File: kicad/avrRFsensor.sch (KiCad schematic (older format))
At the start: 26 parts, among them P1 CONN_1, P2 CONN_1, P3 CONN_1, P4 CONN_1, P5 CONN_1, P6 CONN_1, U1 ATMEGA168PA-A, U2 RFM69, X1 18MHz HC49USSMD

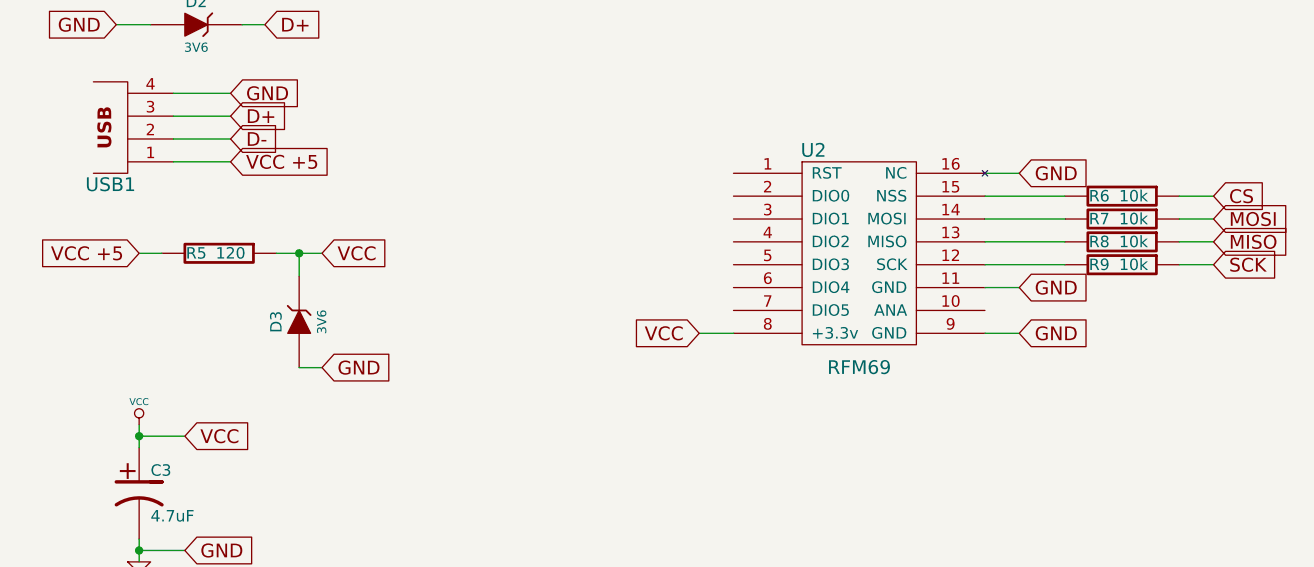
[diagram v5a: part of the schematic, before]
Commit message: fixed schematics. Working hidtool, transmit and read RFM registers in test mode.
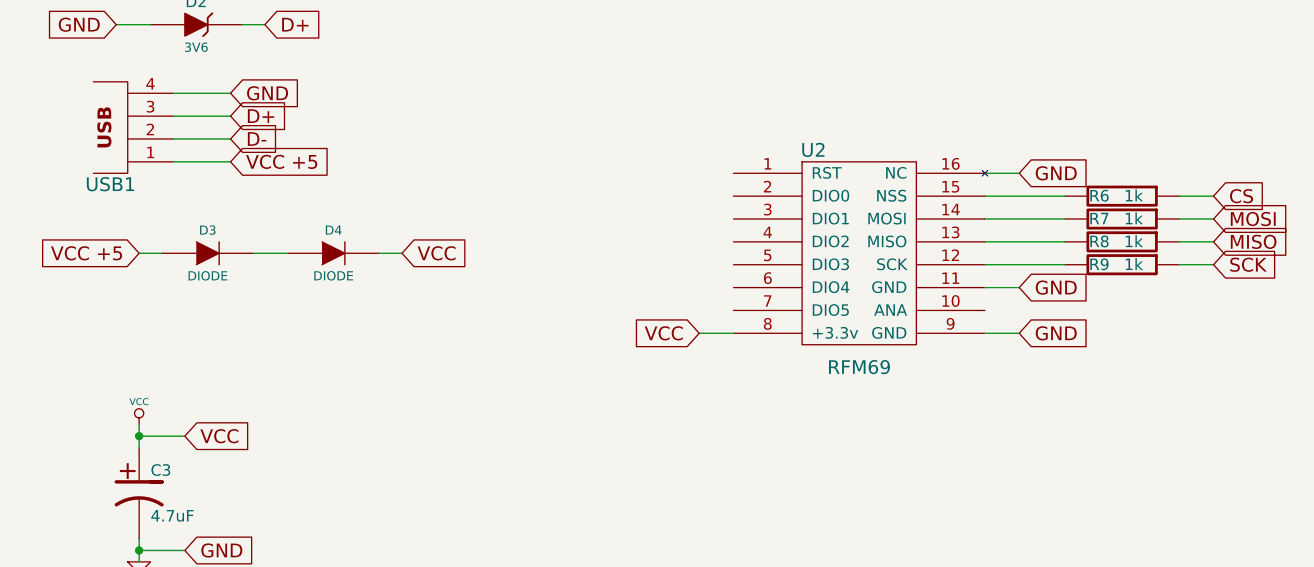
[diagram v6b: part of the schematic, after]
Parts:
- removed D3: 3V6, symbol ZENER
- removed R5: 120, symbol R
- added D3, D4: DIODE, ~, symbol DIODE
- R6, R7, R8, R9: value 10k -> 1k
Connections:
- net VCC: now also D4.2 (K)
- net VCC +5: now also D3.1 (A)
- new net: D3.2 (K), D4.1 (A)
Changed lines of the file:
@@
 Sheet 1 1
 Title ""
-Date "26 jan 2015"
+Date "7 feb 2015"
 Rev ""
 Comp ""
@@
 $EndComp
 $Comp
-L GND #PWR01
+L GND #PWR2
 U 1 1 4E041C8A
 P 1050 7350
-F 0 "#PWR01" H 1050 7350 30  0001 C CNN
+F 0 "#PWR2" H 1050 7350 30  0001 C CNN
 F 1 "GND" H 1050 7280 30  0001 C CNN
 F 2 "" H 1050 7350 60  0001 C CNN
@@
 Connection ~ 1050 6800
 $Comp
-L VCC #PWR02
+L VCC #PWR1
 U 1 1 54B791F6
 P 1050 6750
-F 0 "#PWR02" H 1050 6850 30  0001 C CNN
+F 0 "#PWR1" H 1050 6850 30  0001 C CNN
 F 1 "VCC" H 1050 6850 30  0000 C CNN
 F 2 "" H 1050 6750 60  0000 C CNN
@@
 P 5350 5850
 F 0 "R7" V 5350 5750 50  0000 C CNN
-F 1 "10k" V 5350 5900 50  0000 C CNN
+F 1 "1k" V 5350 5900 50  0000 C CNN
 F 2 "" H 5350 5850 60  0001 C CNN
 F 3 "" H 5350 5850 60  0001 C CNN
@@
 P 5350 5950
 F 0 "R8" V 5350 5850 50  0000 C CNN
-F 1 "10k" V 5350 6000 50  0000 C CNN
+F 1 "1k" V 5350 6000 50  0000 C CNN
 F 2 "" H 5350 5950 60  0001 C CNN
 F 3 "" H 5350 5950 60  0001 C CNN
@@
 P 5350 6050
 F 0 "R9" V 5350 5950 50  0000 C CNN
-F 1 "10k" V 5350 6100 50  0000 C CNN
+F 1 "1k" V 5350 6100 50  0000 C CNN
 F 2 "" H 5350 6050 60  0001 C CNN
 F 3 "" H 5350 6050 60  0001 C CNN
@@
 Text GLabel 1050 6000 0    60   Input ~ 0
 VCC +5
-$Comp
-L R R5
-U 1 1 54B7D03F
-P 1400 6000
-F 0 "R5" V 1400 5900 50  0000 C CNN
-F 1 "120" V 1400 6050 50  0000 C CNN
-F 2 "" H 1400 6000 60  0001 C CNN
-F 3 "" H 1400 6000 60  0001 C CNN
-	1    1400 6000
-	0    1    1    0
-$EndComp
-$Comp
-L ZENER D3
-U 1 1 54B7D045
-P 1750 6300
-F 0 "D3" H 1750 6400 50  0000 C CNN
-F 1 "3V6" H 1750 6200 40  0000 C CNN
-F 2 "" H 1750 6300 60  0001 C CNN
-F 3 "" H 1750 6300 60  0001 C CNN
-	1    1750 6300
-	0    -1   -1   0
-$EndComp
-Text GLabel 1850 6000 2    60   Input ~ 0
+Text GLabel 2200 6000 2    60   Input ~ 0
 VCC
 Wire Wire Line
 	1050 6000 1150 6000
-Wire Wire Line
-	1650 6000 1850 6000
-Wire Wire Line
-	1750 6100 1750 6000
-Connection ~ 1750 6000
-Text GLabel 1850 6500 2    60   Input ~ 0
-GND
-Wire Wire Line
-	1750 6500 1850 6500
 $Comp
 L R R6
@@
 P 5350 5750
 F 0 "R6" V 5350 5650 50  0000 C CNN
-F 1 "10k" V 5350 5800 50  0000 C CNN
+F 1 "1k" V 5350 5800 50  0000 C CNN
 F 2 "" H 5350 5750 60  0001 C CNN
 F 3 "" H 5350 5750 60  0001 C CNN
@@
 Wire Wire Line
 	6300 4600 5300 4600
+$Comp
+L DIODE D3
+U 1 1 54D5C585
+P 1350 6000
+F 0 "D3" H 1350 6100 40  0000 C CNN
+F 1 "DIODE" H 1350 5900 40  0000 C CNN
+F 2 "~" H 1350 6000 60  0000 C CNN
+F 3 "~" H 1350 6000 60  0000 C CNN
+	1    1350 6000
+	1    0    0    -1
+$EndComp
+$Comp
+L DIODE D4
+U 1 1 54D5C594
+P 1900 6000
+F 0 "D4" H 1900 6100 40  0000 C CNN
+F 1 "DIODE" H 1900 5900 40  0000 C CNN
+F 2 "~" H 1900 6000 60  0000 C CNN
+F 3 "~" H 1900 6000 60  0000 C CNN
+	1    1900 6000
+	1    0    0    -1
+$EndComp
+Wire Wire Line
+	1550 6000 1700 6000
+Wire Wire Line
+	2100 6000 2200 6000
 $EndSCHEMATC

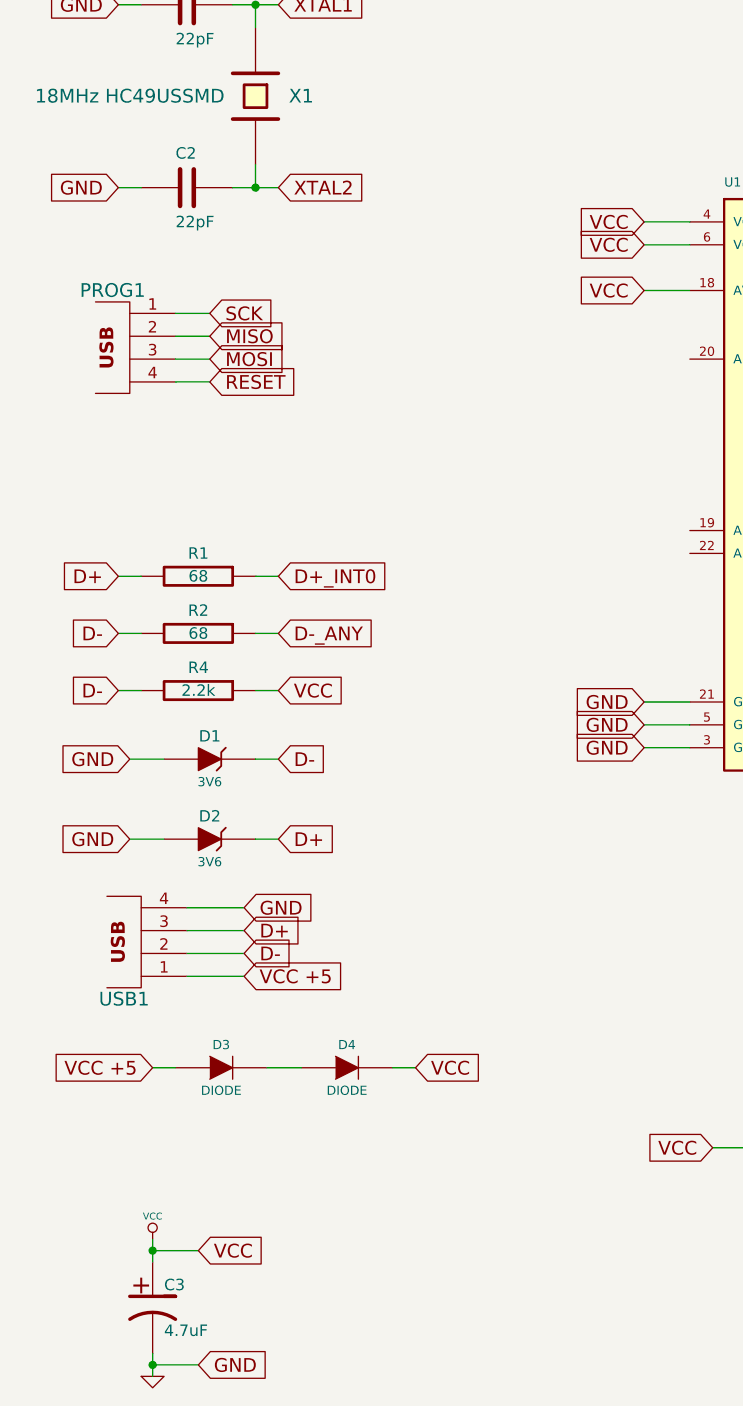
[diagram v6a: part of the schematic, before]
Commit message: No diodes inside module. They are now in the cable. So device should not be used directly in the USB port of computer.
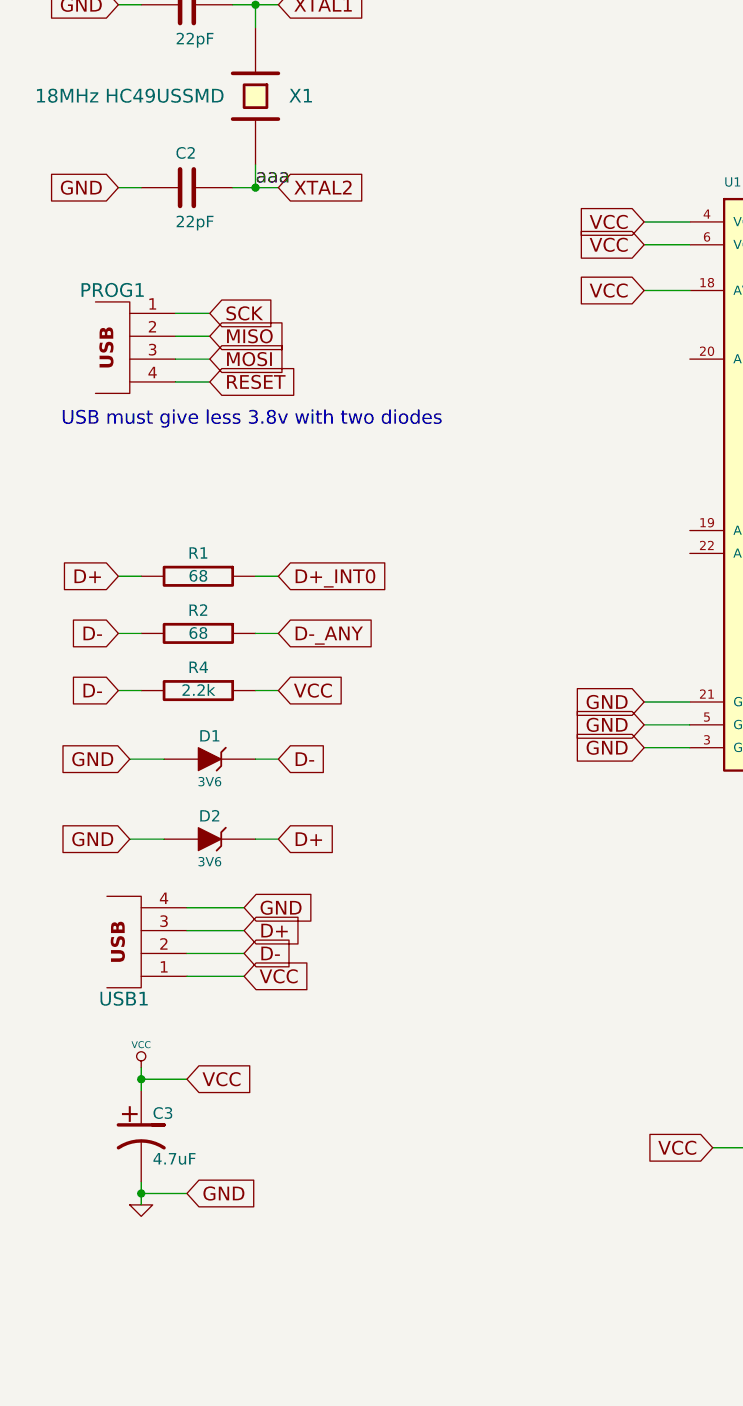
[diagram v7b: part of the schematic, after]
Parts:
- removed D3, D4: DIODE, ~, symbol DIODE
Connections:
- net VCC +5 is gone; now on net VCC: USB1.1
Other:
- note added: "USB must give less 3.8v with two diodes"
- moved on the sheet: C3
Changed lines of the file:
@@
 Sheet 1 1
 Title ""
-Date "7 feb 2015"
+Date "10 feb 2015"
 Rev ""
 Comp ""
@@
 Wire Wire Line
 	1500 1350 1500 1450
-Connection ~ 1050 7300
+Connection ~ 1000 6550
 Wire Wire Line
 	950  4650 1100 4650
@@
 L GND #PWR2
 U 1 1 4E041C8A
-P 1050 7350
-F 0 "#PWR2" H 1050 7350 30  0001 C CNN
-F 1 "GND" H 1050 7280 30  0001 C CNN
-F 2 "" H 1050 7350 60  0001 C CNN
-F 3 "" H 1050 7350 60  0001 C CNN
-	1    1050 7350
+P 1000 6600
+F 0 "#PWR2" H 1000 6600 30  0001 C CNN
+F 1 "GND" H 1000 6530 30  0001 C CNN
+F 2 "" H 1000 6600 60  0001 C CNN
+F 3 "" H 1000 6600 60  0001 C CNN
+	1    1000 6600
 	1    0    0    -1
 $EndComp
@@
 L CP1 C3
 U 1 1 4B61D8DC
-P 1050 7050
-F 0 "C3" H 1100 7150 50  0000 L CNN
-F 1 "4.7uF" H 1100 6950 50  0000 L CNN
-F 2 "" H 1050 7050 60  0001 C CNN
-F 3 "" H 1050 7050 60  0001 C CNN
-	1    1050 7050
+P 1000 6300
+F 0 "C3" H 1050 6400 50  0000 L CNN
+F 1 "4.7uF" H 1050 6200 50  0000 L CNN
+F 2 "" H 1000 6300 60  0001 C CNN
+F 3 "" H 1000 6300 60  0001 C CNN
+	1    1000 6300
 	1    0    0    -1
 $EndComp
@@
 	1    0    0    -1
 $EndComp
-Text GLabel 1250 6800 2    60   Input ~ 0
+Text GLabel 1200 6050 2    60   Input ~ 0
 VCC
 Text GLabel 1600 4350 2    60   Input ~ 0
@@
 Wire Wire Line
 	1000 1000 1100 1000
-Text GLabel 1250 7300 2    60   Input ~ 0
+Text GLabel 1200 6550 2    60   Input ~ 0
 GND
 Text GLabel 900  1350 0    60   Input ~ 0
@@
 MOSI
 Wire Wire Line
-	1050 7250 1050 7350
-Wire Wire Line
-	1050 6750 1050 6850
-Connection ~ 1050 6800
+	1000 6500 1000 6600
+Wire Wire Line
+	1000 6000 1000 6100
+Connection ~ 1000 6050
 $Comp
 L VCC #PWR1
 U 1 1 54B791F6
-P 1050 6750
-F 0 "#PWR1" H 1050 6850 30  0001 C CNN
-F 1 "VCC" H 1050 6850 30  0000 C CNN
-F 2 "" H 1050 6750 60  0000 C CNN
-F 3 "" H 1050 6750 60  0000 C CNN
-	1    1050 6750
+P 1000 6000
+F 0 "#PWR1" H 1000 6100 30  0001 C CNN
+F 1 "VCC" H 1000 6100 30  0000 C CNN
+F 2 "" H 1000 6000 60  0000 C CNN
+F 3 "" H 1000 6000 60  0000 C CNN
+	1    1000 6000
 	1    0    0    -1
 $EndComp
@@
 	1500 3850 1600 3850
 Text GLabel 1450 5600 2    60   Input ~ 0
-VCC +5
+VCC
 Text GLabel 1450 5300 2    60   Input ~ 0
 GND
@@
 	5500 2900 5300 2900
 Wire Wire Line
-	1250 7300 1050 7300
-Wire Wire Line
-	1250 6800 1050 6800
+	1200 6550 1000 6550
+Wire Wire Line
+	1200 6050 1000 6050
 Text GLabel 3200 4600 0    60   Input ~ 0
 GND
@@
 Wire Wire Line
 	5600 5850 5750 5850
-Text GLabel 1050 6000 0    60   Input ~ 0
-VCC +5
-Text GLabel 2200 6000 2    60   Input ~ 0
-VCC
-Wire Wire Line
-	1050 6000 1150 6000
 $Comp
 L R R6
@@
 Wire Wire Line
 	6300 4600 5300 4600
-$Comp
-L DIODE D3
-U 1 1 54D5C585
-P 1350 6000
-F 0 "D3" H 1350 6100 40  0000 C CNN
-F 1 "DIODE" H 1350 5900 40  0000 C CNN
-F 2 "~" H 1350 6000 60  0000 C CNN
-F 3 "~" H 1350 6000 60  0000 C CNN
-	1    1350 6000
-	1    0    0    -1
-$EndComp
-$Comp
-L DIODE D4
-U 1 1 54D5C594
-P 1900 6000
-F 0 "D4" H 1900 6100 40  0000 C CNN
-F 1 "DIODE" H 1900 5900 40  0000 C CNN
-F 2 "~" H 1900 6000 60  0000 C CNN
-F 3 "~" H 1900 6000 60  0000 C CNN
-	1    1900 6000
-	1    0    0    -1
-$EndComp
-Wire Wire Line
-	1550 6000 1700 6000
-Wire Wire Line
-	2100 6000 2200 6000
+Text Label 1500 2150 0    60   ~ 0
+aaa
+Text Notes 650  3200 0    60   ~ 0
+USB must give less 3.8v with two diodes
 $EndSCHEMATC

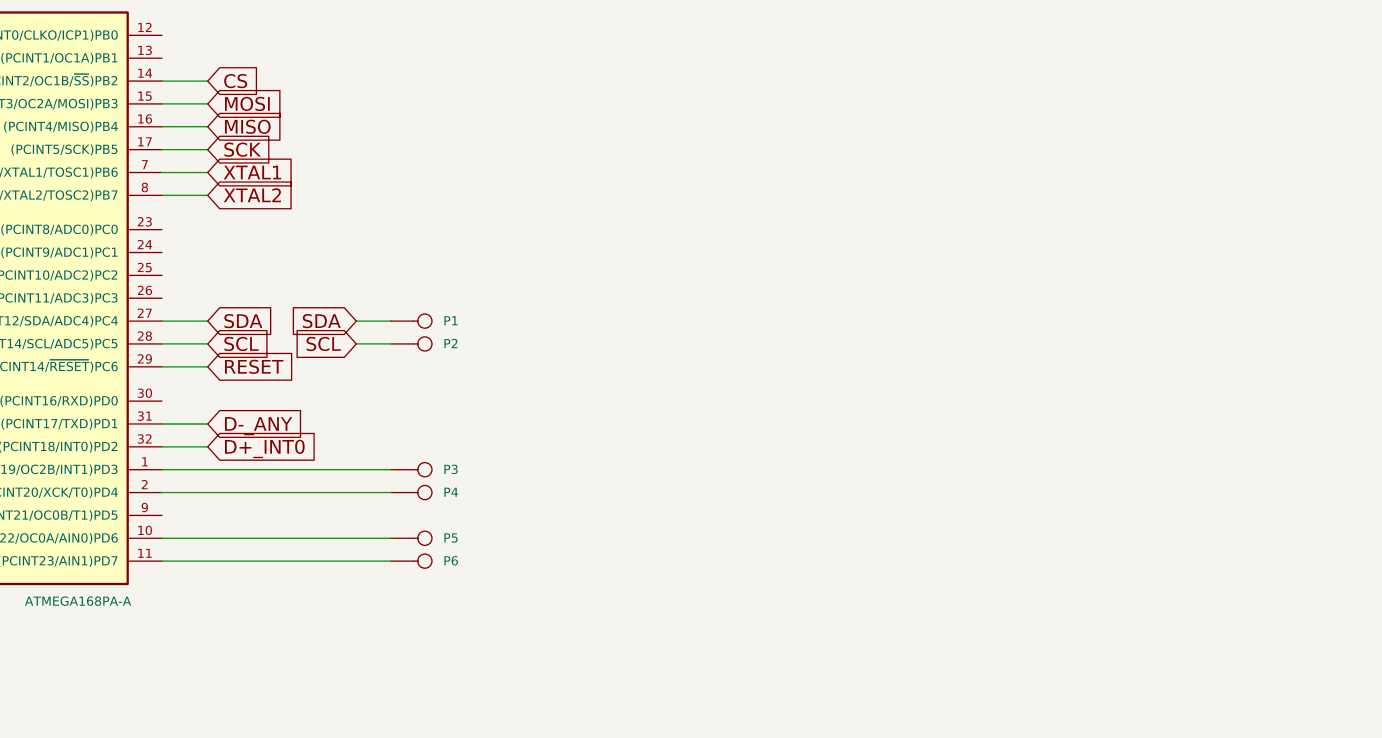
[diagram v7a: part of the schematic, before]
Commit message: Changed Quartz to low profile one XT324 added Comparator related parts
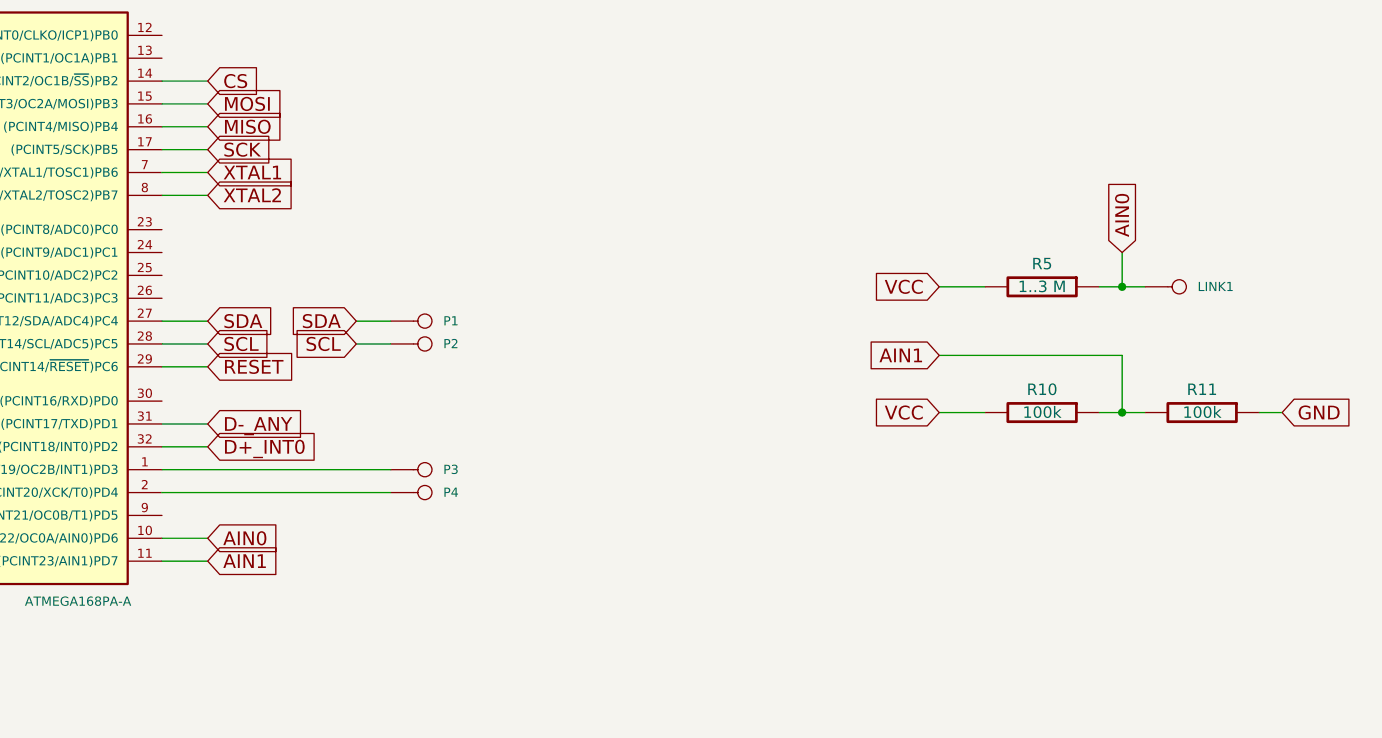
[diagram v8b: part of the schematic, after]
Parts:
- removed P6: CONN_1, symbol CONN_1
- added R10, R11: 100k, symbol R
- added R5: 1..3 M, symbol R
- renumbered P5 to LINK1
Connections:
- net GND: now also R11.1
- net VCC: now also R10.2, R5.2
- net AIN0: now reaches LINK1.1, U1.10 ((PCINT22/OC0A/AIN0)PD6)
- net AIN0: now also R5.1
- net AIN1: now reaches U1.11 ((PCINT23/AIN1)PD7)
- net AIN1: now also R10.1, R11.2
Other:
- moved on the sheet: LINK1
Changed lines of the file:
@@
 Sheet 1 1
 Title ""
-Date "10 feb 2015"
+Date "10 may 2015"
 Rev ""
 Comp ""
@@
 	5300 4300 6300 4300
 $Comp
-L CONN_1 P5
+L CONN_1 LINK1
 U 1 1 54BA884D
-P 6450 4500
-F 0 "P5" H 6530 4500 40  0000 L CNN
-F 1 "CONN_1" H 6450 4555 30  0001 C CNN
-F 2 "" H 6450 4500 60  0000 C CNN
-F 3 "" H 6450 4500 60  0000 C CNN
-	1    6450 4500
-	1    0    0    -1
-$EndComp
-Wire Wire Line
-	6300 4500 5300 4500
-$Comp
-L CONN_1 P6
-U 1 1 54BA88D5
-P 6450 4600
-F 0 "P6" H 6530 4600 40  0000 L CNN
-F 1 "CONN_1" H 6450 4655 30  0001 C CNN
-F 2 "" H 6450 4600 60  0000 C CNN
-F 3 "" H 6450 4600 60  0000 C CNN
-	1    6450 4600
-	1    0    0    -1
-$EndComp
-Wire Wire Line
-	6300 4600 5300 4600
+P 9750 3400
+F 0 "LINK1" H 9830 3400 40  0000 L CNN
+F 1 "CONN_1" H 9750 3455 30  0001 C CNN
+F 2 "" H 9750 3400 60  0000 C CNN
+F 3 "" H 9750 3400 60  0000 C CNN
+	1    9750 3400
+	1    0    0    -1
+$EndComp
 Text Label 1500 2150 0    60   ~ 0
 aaa
 Text Notes 650  3200 0    60   ~ 0
 USB must give less 3.8v with two diodes
+Text GLabel 5500 4500 2    60   Input ~ 0
+AIN0
+Text GLabel 5500 4600 2    60   Input ~ 0
+AIN1
+Wire Wire Line
+	5300 4500 5500 4500
+Wire Wire Line
+	5300 4600 5500 4600
+Text GLabel 9500 3250 1    60   Input ~ 0
+AIN0
+Text GLabel 8700 3700 0    60   Input ~ 0
+AIN1
+$Comp
+L R R5
+U 1 1 554F1B91
+P 9150 3400
+F 0 "R5" V 9050 3400 50  0000 C CNN
+F 1 "1..3 M" V 9150 3400 50  0000 C CNN
+F 2 "" H 9150 3400 60  0001 C CNN
+F 3 "" H 9150 3400 60  0001 C CNN
+	1    9150 3400
+	0    1    1    0
+$EndComp
+Text GLabel 10200 3950 2    60   Input ~ 0
+GND
+Text GLabel 8700 3400 0    60   Input ~ 0
+VCC
+Text GLabel 8700 3950 0    60   Input ~ 0
+VCC
+$Comp
+L R R11
+U 1 1 554F1BBC
+P 9850 3950
+F 0 "R11" V 9750 3950 50  0000 C CNN
+F 1 "100k" V 9850 3950 50  0000 C CNN
+F 2 "" H 9850 3950 60  0001 C CNN
+F 3 "" H 9850 3950 60  0001 C CNN
+	1    9850 3950
+	0    1    1    0
+$EndComp
+$Comp
+L R R10
+U 1 1 554F1BC2
+P 9150 3950
+F 0 "R10" V 9050 3950 50  0000 C CNN
+F 1 "100k" V 9150 3950 50  0000 C CNN
+F 2 "" H 9150 3950 60  0001 C CNN
+F 3 "" H 9150 3950 60  0001 C CNN
+	1    9150 3950
+	0    1    1    0
+$EndComp
+Wire Wire Line
+	9600 3400 9400 3400
+Wire Wire Line
+	9500 3400 9500 3250
+Connection ~ 9500 3400
+Wire Wire Line
+	8900 3400 8700 3400
+Wire Wire Line
+	10200 3950 10100 3950
+Wire Wire Line
+	9600 3950 9400 3950
+Wire Wire Line
+	8900 3950 8700 3950
+Wire Wire Line
+	8700 3700 9500 3700
+Wire Wire Line
+	9500 3700 9500 3950
+Connection ~ 9500 3950
 $EndSCHEMATC
